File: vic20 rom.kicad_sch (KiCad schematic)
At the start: 8 parts, among them J1 Kernel C/E Pin 20, J2 Basic Bank 2 S/W, J3 Basic Bank 2 S/W, J4 Kernel Bank 2 S/W, J5 Kernel Bank 2 S/W, U1 27C256, U2 8K ROM, U3 74LS08

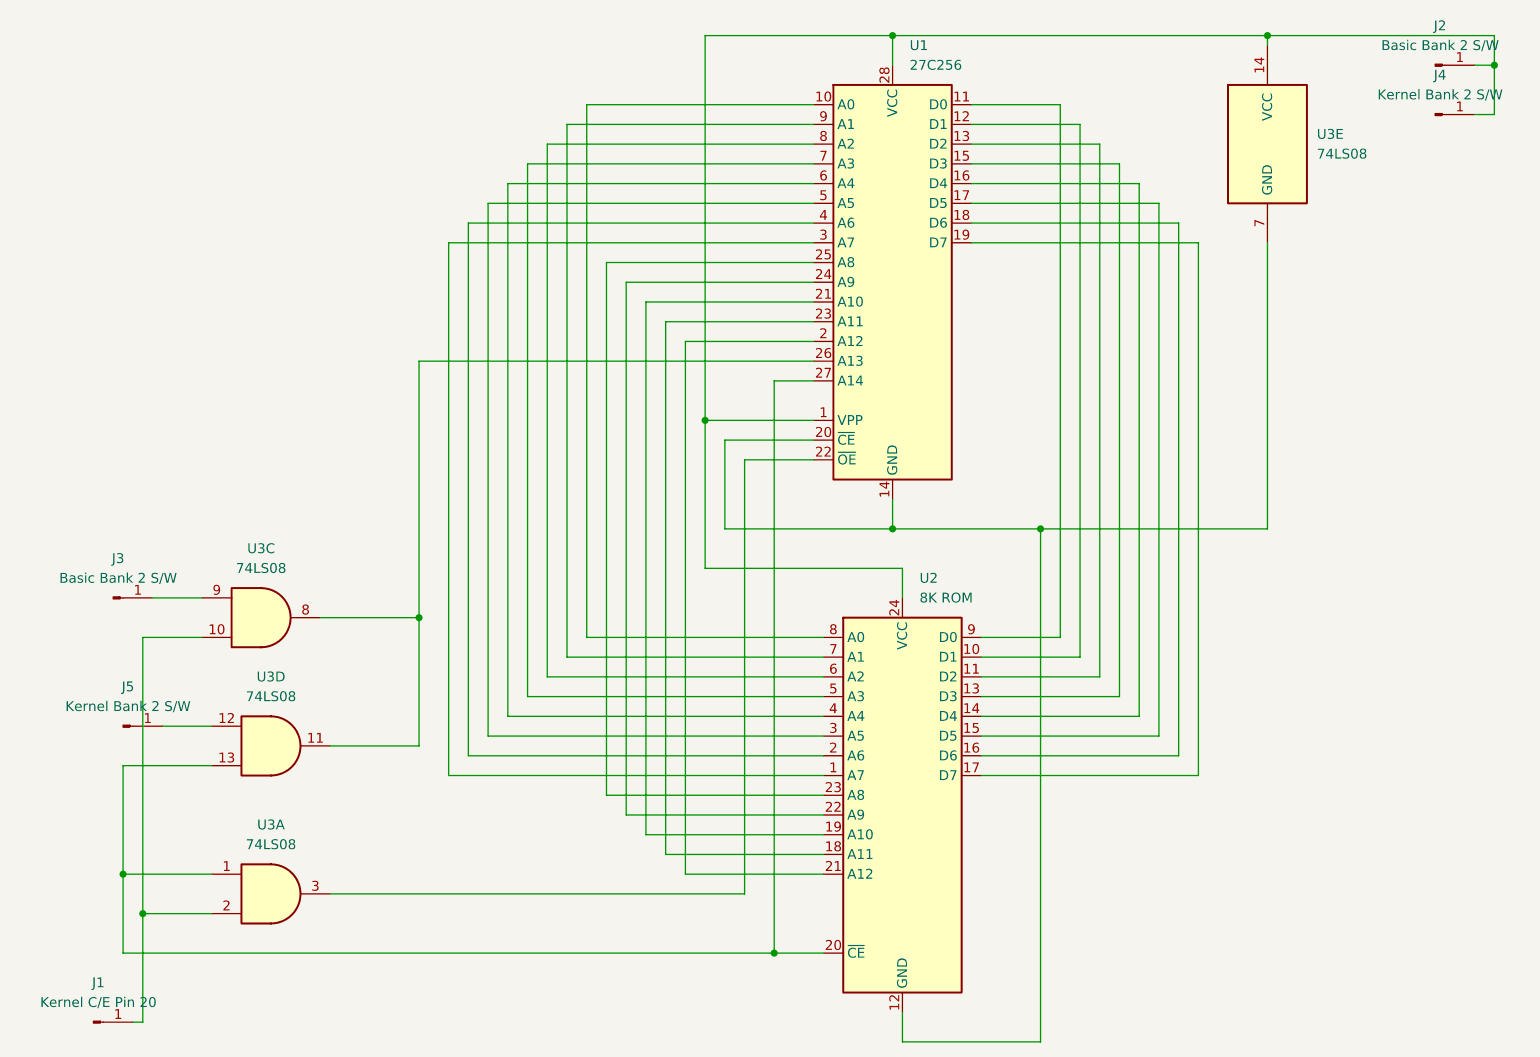
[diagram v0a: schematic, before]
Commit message: Master: Added GND pin for switches
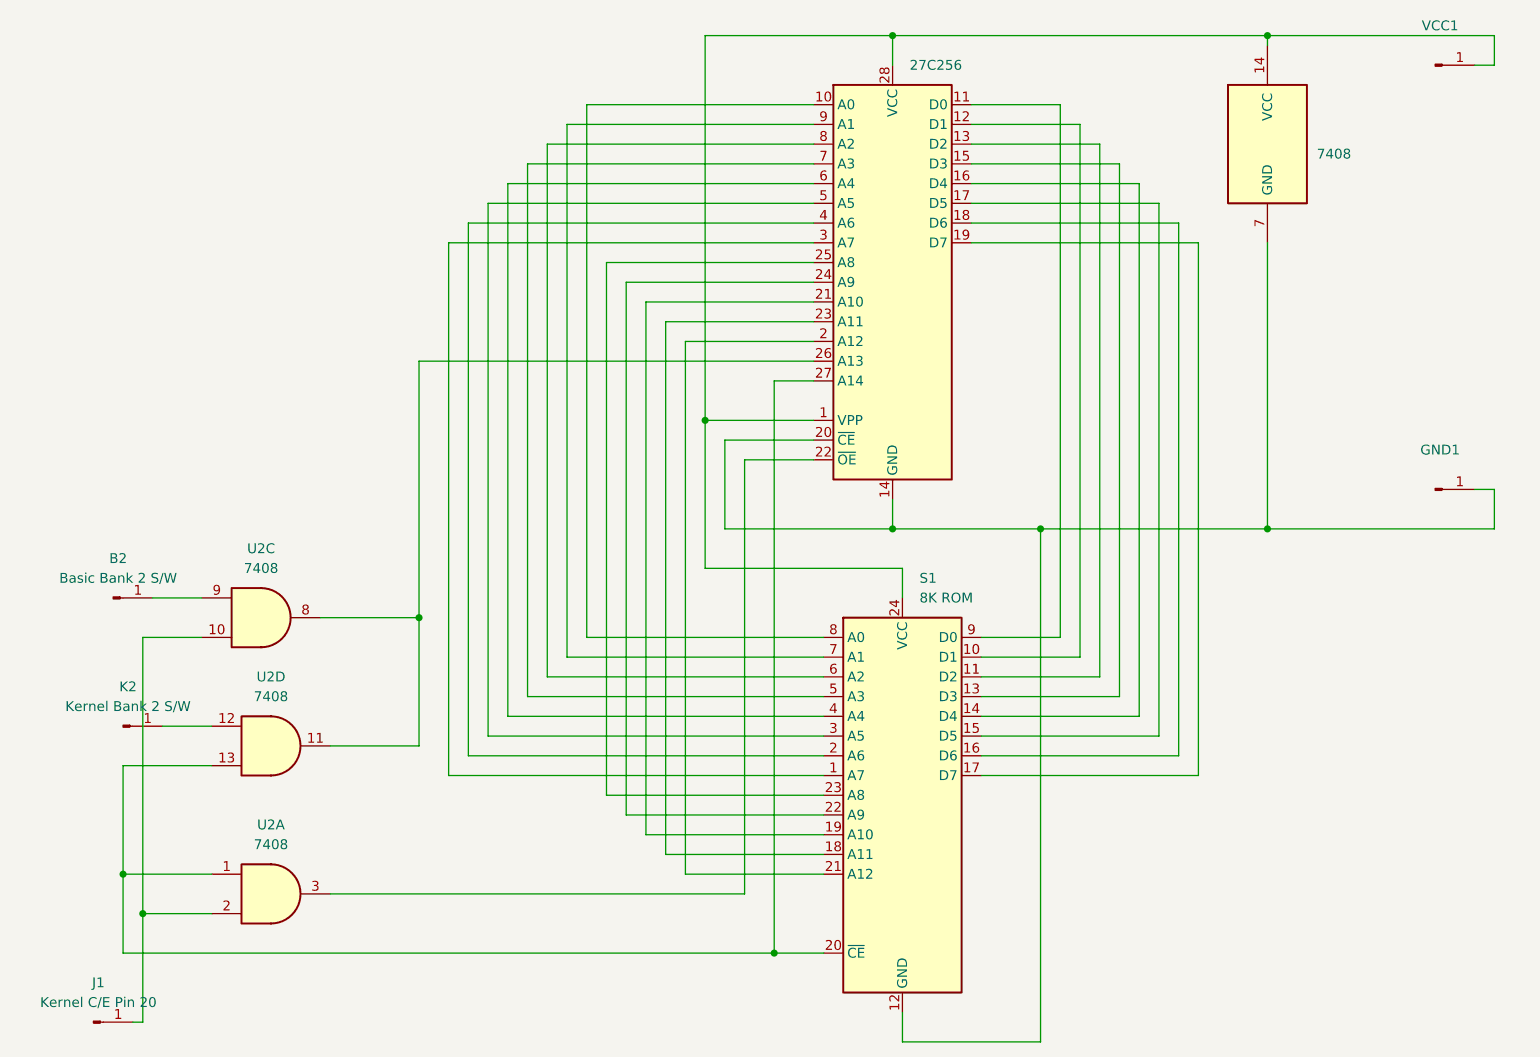
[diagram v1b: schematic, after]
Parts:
- removed J4: Kernel Bank 2 S/W, Connector_Pin:Pin_D0.7mm_L6.5mm_W1.8mm_FlatFork, symbol Connector:Conn_01x01_Pin
- added GND1: S/W GND, Connector_Pin:Pin_D0.7mm_L6.5mm_W1.8mm_FlatFork, symbol Connector:Conn_01x01_Pin
- U2: renamed from U3; value 74LS08 -> 7408
- VCC1: renamed from J2; value Basic Bank 2 S/W -> S/W VCC
- renumbered J3 to B2, J5 to K2, U2 to S1
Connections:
- net at S1.12 (GND), U1.14 (GND), U1.20 (~{CE})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: now also GND1.1 (Pin_1)
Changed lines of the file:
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@@
   (junction (at 127 85.09) (diameter 0) (color 0 0 0 0)
   )
-  (junction (at 204.47 25.4) (diameter 0) (color 0 0 0 0)
-  )
   (junction (at 102.87 71.12) (diameter 0) (color 0 0 0 0)
   )
   (junction (at 30.48 134.62) (diameter 0) (color 0 0 0 0)
   )
+  (junction (at 175.26 85.09) (diameter 0) (color 0 0 0 0)
+  )
   (junction (at 146.05 85.09) (diameter 0) (color 0 0 0 0)
   )
@@
     (stroke (width 0) (type default))
   )
-  (wire (pts (xy 204.47 25.4) (xy 204.47 31.75))
+  (wire (pts (xy 204.47 85.09) (xy 175.26 85.09))
     (stroke (width 0) (type default))
   )
@@
     (stroke (width 0) (type default))
   )
+  (wire (pts (xy 204.47 80.01) (xy 204.47 85.09))
+    (stroke (width 0) (type default))
+  )
   (wire (pts (xy 74.93 111.76) (xy 74.93 43.18))
     (stroke (width 0) (type default))
@@
     (stroke (width 0) (type default))
   )
-  (wire (pts (xy 201.93 31.75) (xy 204.47 31.75))
+  (wire (pts (xy 201.93 80.01) (xy 204.47 80.01))
     (stroke (width 0) (type default))
   )
@@
   (symbol (lib_id "Memory_EPROM:27C64") (at 128.27 119.38 0) (unit 1)
     (in_bom yes) (on_board yes) (dnp no) (fields_autoplaced)
-    (property "Reference" "U2" (at 130.4641 91.44 0)
+    (property "Reference" "S1" (at 130.4641 91.44 0)
       (effects (font (size 1.27 1.27)) (justify left))
     )
@@
       (project "vic20 rom"
         (path "/c8ce4b53-0fb8-4d08-ae87-6be1b4893983"
-          (reference "U2") (unit 1)
+          (reference "S1") (unit 1)
         )
       )
@@
   (symbol (lib_id "74xx:74LS08") (at 46.99 113.03 0) (unit 4)
     (in_bom yes) (on_board yes) (dnp no) (fields_autoplaced)
-    (property "Reference" "U3" (at 46.9817 104.14 0)
-      (effects (font (size 1.27 1.27)))
-    )
-    (property "Value" "74LS08" (at 46.9817 106.68 0)
+    (property "Reference" "U2" (at 46.9817 104.14 0)
+      (effects (font (size 1.27 1.27)))
+    )
+    (property "Value" "7408" (at 46.9817 106.68 0)
       (effects (font (size 1.27 1.27)))
     )
@@
       (project "vic20 rom"
         (path "/c8ce4b53-0fb8-4d08-ae87-6be1b4893983"
-          (reference "U3") (unit 4)
+          (reference "U2") (unit 4)
         )
       )
@@
     (in_bom yes) (on_board yes) (dnp no) (fields_autoplaced)
     (property "Reference" "U1" (at 129.1941 22.86 0)
-      (effects (font (size 1.27 1.27)) (justify left))
+      (effects (font (size 1.27 1.27)) (justify left) hide)
     )
     (property "Value" "27C256" (at 129.1941 25.4 0)
@@
   (symbol (lib_id "Connector:Conn_01x01_Pin") (at 26.67 93.98 0) (unit 1)
     (in_bom yes) (on_board yes) (dnp no)
-    (property "Reference" "J3" (at 27.305 88.9 0)
+    (property "Reference" "B2" (at 27.305 88.9 0)
       (effects (font (size 1.27 1.27)))
     )
@@
       (project "vic20 rom"
         (path "/c8ce4b53-0fb8-4d08-ae87-6be1b4893983"
-          (reference "J3") (unit 1)
+          (reference "B2") (unit 1)
+        )
+      )
+    )
+  )
+  (symbol (lib_id "Connector:Conn_01x01_Pin") (at 196.85 80.01 0) (unit 1)
+    (in_bom yes) (on_board yes) (dnp no)
+    (property "Reference" "GND1" (at 197.485 74.93 0)
+      (effects (font (size 1.27 1.27)))
+    )
+    (property "Value" "S/W GND" (at 197.485 77.47 0)
+      (effects (font (size 1.27 1.27)) hide)
+    )
+    (property "Footprint" "Connector_Pin:Pin_D0.7mm_L6.5mm_W1.8mm_FlatFork" (at 196.85 80.01 0)
+      (effects (font (size 1.27 1.27)) hide)
+    )
+    (property "Datasheet" "~" (at 196.85 80.01 0)
+      (effects (font (size 1.27 1.27)) hide)
+    )
+    (pin "1")
+    (instances
+      (project "vic20 rom"
+        (path "/c8ce4b53-0fb8-4d08-ae87-6be1b4893983"
+          (reference "GND1") (unit 1)
         )
       )
@@
   (symbol (lib_id "74xx:74LS08") (at 46.99 132.08 0) (unit 1)
     (in_bom yes) (on_board yes) (dnp no) (fields_autoplaced)
-    (property "Reference" "U3" (at 46.9817 123.19 0)
-      (effects (font (size 1.27 1.27)))
-    )
-    (property "Value" "74LS08" (at 46.9817 125.73 0)
+    (property "Reference" "U2" (at 46.9817 123.19 0)
+      (effects (font (size 1.27 1.27)))
+    )
+    (property "Value" "7408" (at 46.9817 125.73 0)
       (effects (font (size 1.27 1.27)))
     )
@@
       (project "vic20 rom"
         (path "/c8ce4b53-0fb8-4d08-ae87-6be1b4893983"
-          (reference "U3") (unit 1)
+          (reference "U2") (unit 1)
         )
       )
@@
   (symbol (lib_id "74xx:74LS08") (at 45.72 96.52 0) (unit 3)
     (in_bom yes) (on_board yes) (dnp no) (fields_autoplaced)
-    (property "Reference" "U3" (at 45.7117 87.63 0)
-      (effects (font (size 1.27 1.27)))
-    )
-    (property "Value" "74LS08" (at 45.7117 90.17 0)
+    (property "Reference" "U2" (at 45.7117 87.63 0)
+      (effects (font (size 1.27 1.27)))
+    )
+    (property "Value" "7408" (at 45.7117 90.17 0)
       (effects (font (size 1.27 1.27)))
     )
@@
       (project "vic20 rom"
         (path "/c8ce4b53-0fb8-4d08-ae87-6be1b4893983"
-          (reference "U3") (unit 3)
+          (reference "U2") (unit 3)
         )
       )
@@
   (symbol (lib_id "74xx:74LS08") (at 175.26 35.56 0) (unit 5)
     (in_bom yes) (on_board yes) (dnp no) (fields_autoplaced)
-    (property "Reference" "U3" (at 181.61 34.29 0)
-      (effects (font (size 1.27 1.27)) (justify left))
-    )
-    (property "Value" "74LS08" (at 181.61 36.83 0)
+    (property "Reference" "U2" (at 181.61 34.29 0)
+      (effects (font (size 1.27 1.27)) (justify left) hide)
+    )
+    (property "Value" "7408" (at 181.61 36.83 0)
       (effects (font (size 1.27 1.27)) (justify left))
     )
@@
       (project "vic20 rom"
         (path "/c8ce4b53-0fb8-4d08-ae87-6be1b4893983"
-          (reference "U3") (unit 5)
-        )
-      )
-    )
-  )
-  (symbol (lib_id "Connector:Conn_01x01_Pin") (at 196.85 31.75 0) (unit 1)
-    (in_bom yes) (on_board yes) (dnp no)
-    (property "Reference" "J4" (at 197.485 26.67 0)
-      (effects (font (size 1.27 1.27)))
-    )
-    (property "Value" "Kernel Bank 2 S/W" (at 197.485 29.21 0)
-      (effects (font (size 1.27 1.27)))
-    )
-    (property "Footprint" "Connector_Pin:Pin_D0.7mm_L6.5mm_W1.8mm_FlatFork" (at 196.85 31.75 0)
-      (effects (font (size 1.27 1.27)) hide)
-    )
-    (property "Datasheet" "~" (at 196.85 31.75 0)
-      (effects (font (size 1.27 1.27)) hide)
-    )
-    (pin "1")
-    (instances
-      (project "vic20 rom"
-        (path "/c8ce4b53-0fb8-4d08-ae87-6be1b4893983"
-          (reference "J4") (unit 1)
+          (reference "U2") (unit 5)
         )
       )
@@
   (symbol (lib_id "Connector:Conn_01x01_Pin") (at 196.85 25.4 0) (unit 1)
     (in_bom yes) (on_board yes) (dnp no)
-    (property "Reference" "J2" (at 197.485 20.32 0)
-      (effects (font (size 1.27 1.27)))
-    )
-    (property "Value" "Basic Bank 2 S/W" (at 197.485 22.86 0)
-      (effects (font (size 1.27 1.27)))
+    (property "Reference" "VCC1" (at 197.485 20.32 0)
+      (effects (font (size 1.27 1.27)))
+    )
+    (property "Value" "S/W VCC" (at 197.485 22.86 0)
+      (effects (font (size 1.27 1.27)) hide)
     )
     (property "Footprint" "Connector_Pin:Pin_D0.7mm_L6.5mm_W1.8mm_FlatFork" (at 196.85 25.4 0)
@@
       (project "vic20 rom"
         (path "/c8ce4b53-0fb8-4d08-ae87-6be1b4893983"
-          (reference "J2") (unit 1)
+          (reference "VCC1") (unit 1)
         )
       )
@@
   (symbol (lib_id "Connector:Conn_01x01_Pin") (at 27.94 110.49 0) (unit 1)
     (in_bom yes) (on_board yes) (dnp no)
-    (property "Reference" "J5" (at 28.575 105.41 0)
+    (property "Reference" "K2" (at 28.575 105.41 0)
       (effects (font (size 1.27 1.27)))
     )
@@
       (project "vic20 rom"
         (path "/c8ce4b53-0fb8-4d08-ae87-6be1b4893983"
-          (reference "J5") (unit 1)
-        )
-      )
+          (reference "K2") (unit 1)
+        )
+      )

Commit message: Master: Added PCB images to readme file
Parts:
- GND1: value S/W GND -> GND
- VCC1: value S/W VCC -> +5V
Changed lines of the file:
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@@
       (effects (font (size 1.27 1.27)))
     )
-    (property "Value" "S/W GND" (at 197.485 77.47 0)
+    (property "Value" "GND" (at 197.485 77.47 0)
       (effects (font (size 1.27 1.27)) hide)
     )
@@
       (effects (font (size 1.27 1.27)))
     )
-    (property "Value" "S/W VCC" (at 197.485 22.86 0)
+    (property "Value" "+5V" (at 197.485 22.86 0)
       (effects (font (size 1.27 1.27)) hide)
     )
